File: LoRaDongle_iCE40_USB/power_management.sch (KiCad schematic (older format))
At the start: 17 parts

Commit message: initial changes to iCE40UP5k
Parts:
- removed C? (x2): 1uF, symbol Device:C
- removed U?: AP7331-10WG-7, symbol LoRaDongle:AP7331-10WG-7
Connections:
- net labels removed: 1V
- wire segments 66 -> 53
- no-connect marks 1 -> 0
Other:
- moved on the sheet: C?, D?, L?, R?, U?

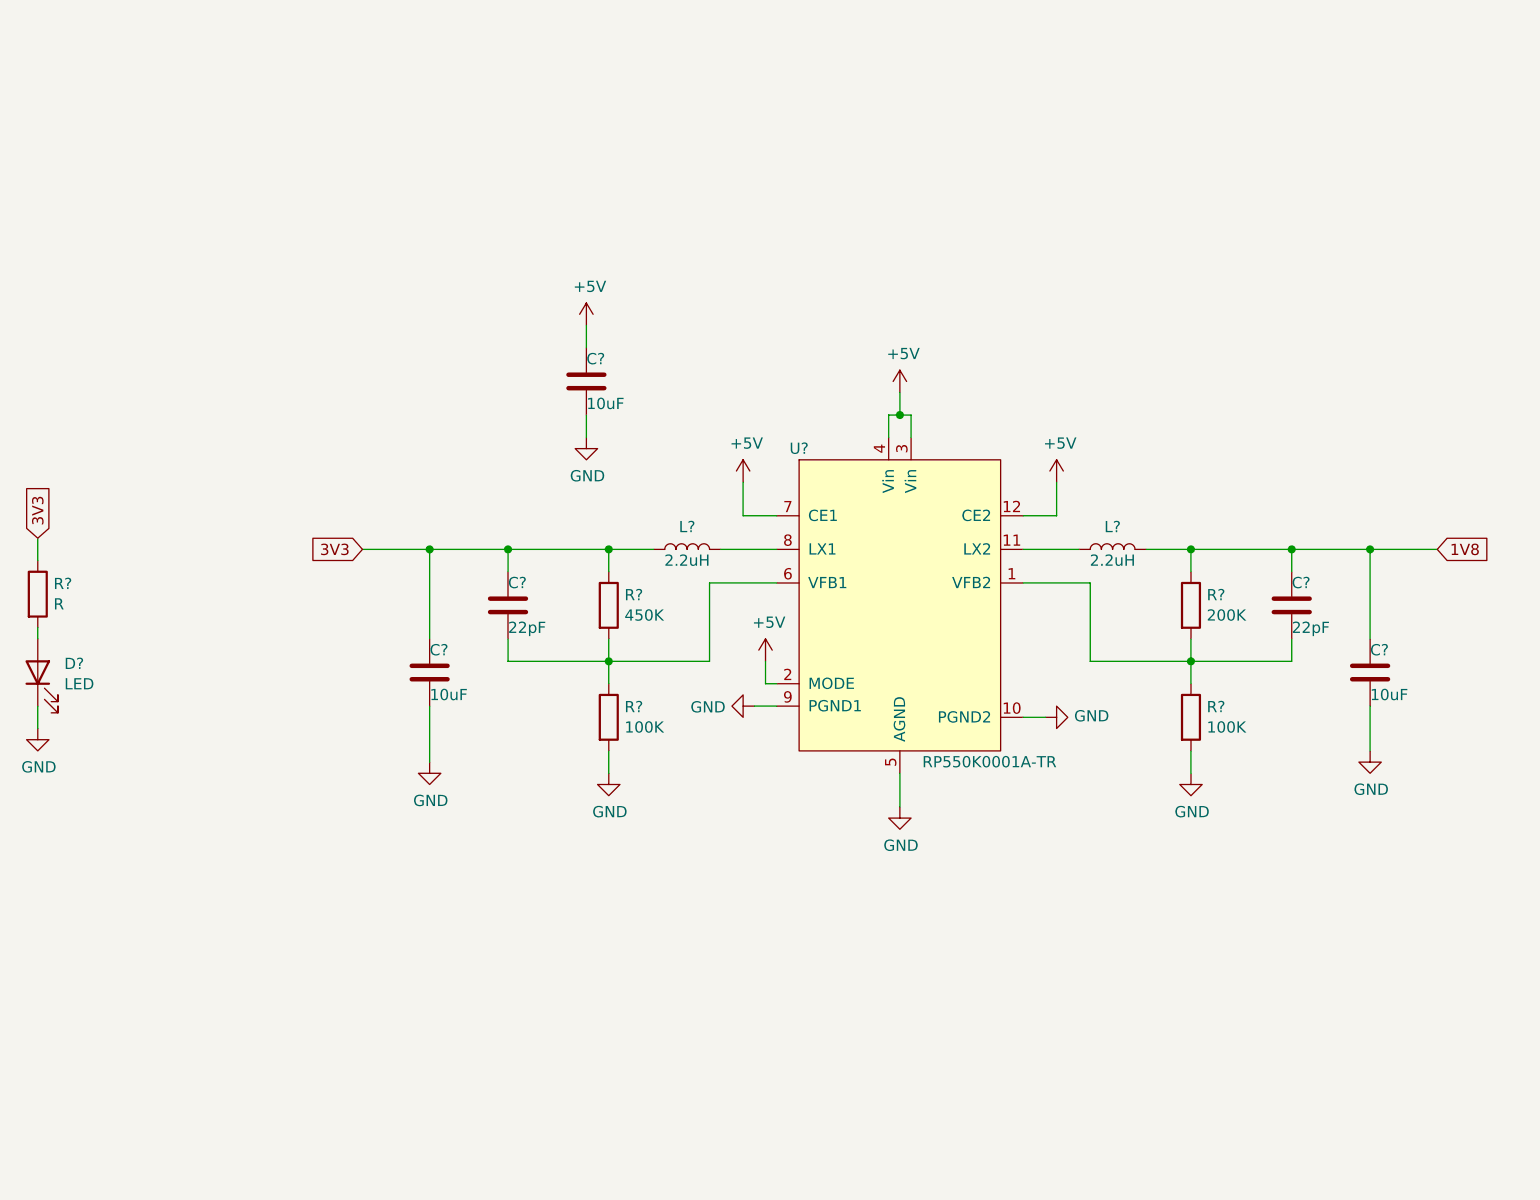
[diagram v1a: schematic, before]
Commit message: changed to sx1261
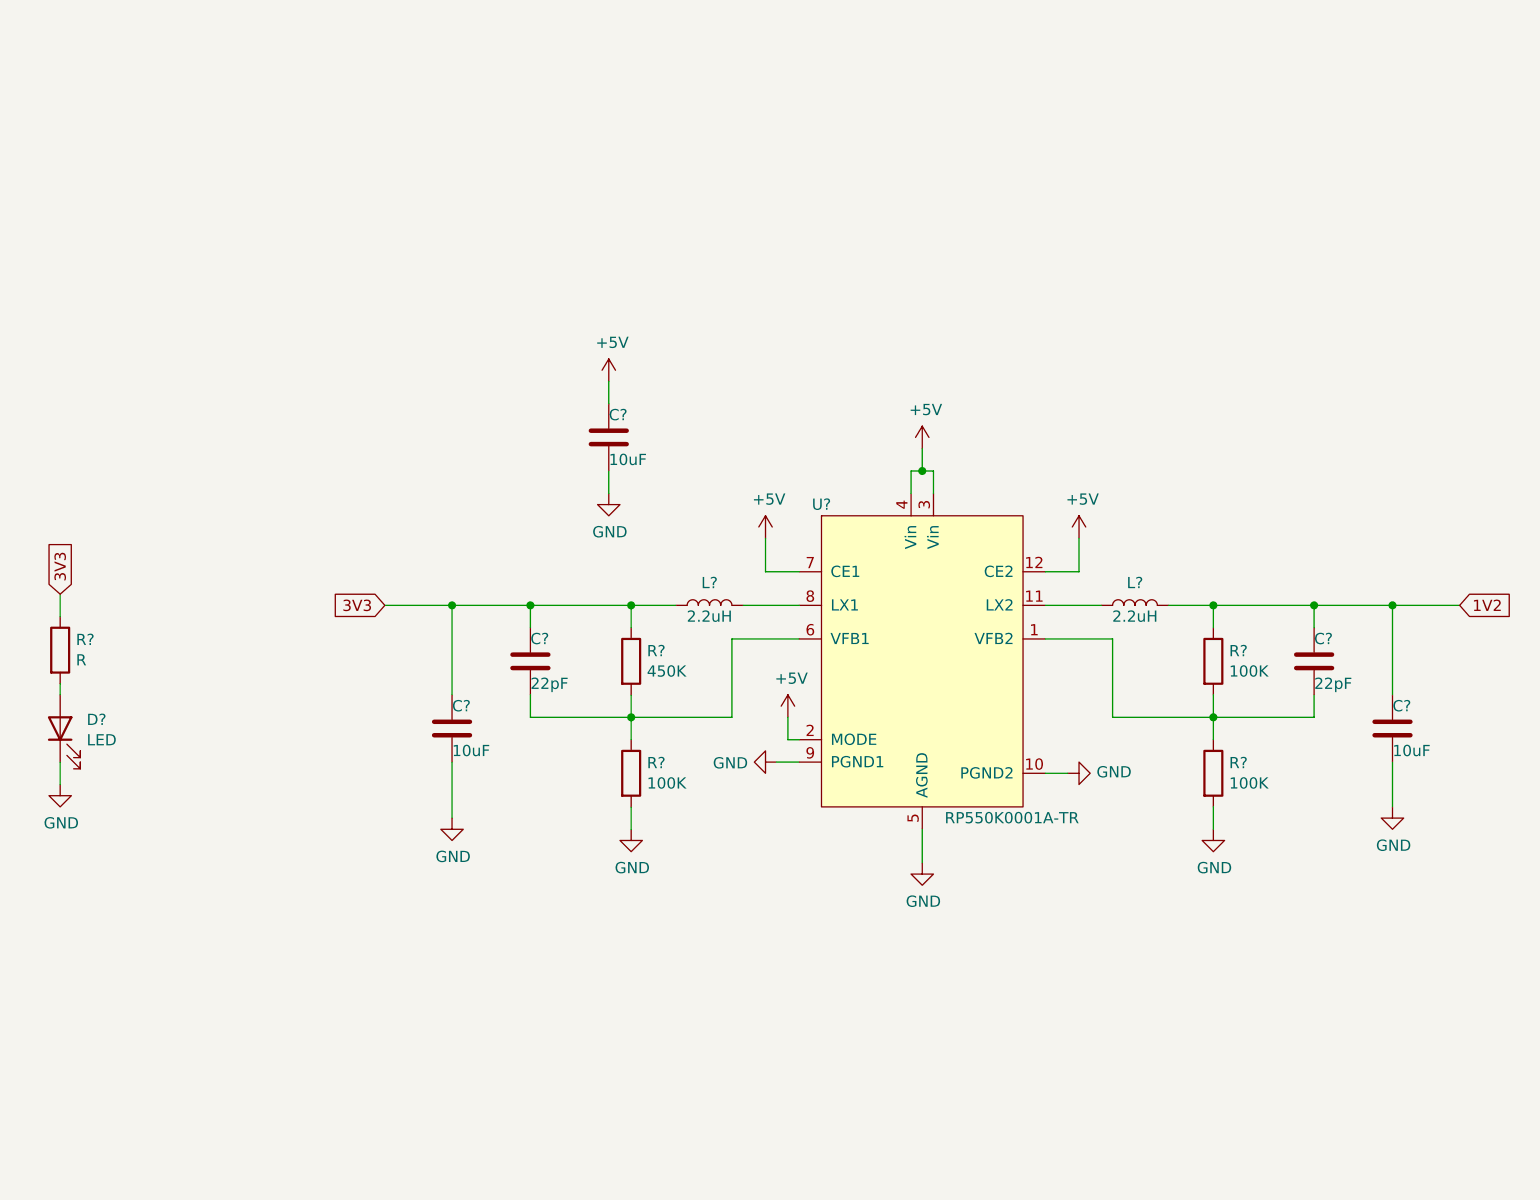
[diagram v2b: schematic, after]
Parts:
- R?: value 200K -> 100K
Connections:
- net 1V8 renamed 1V2
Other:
- moved on the sheet: C?, D?, L?, R?, U?

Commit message: added footprints
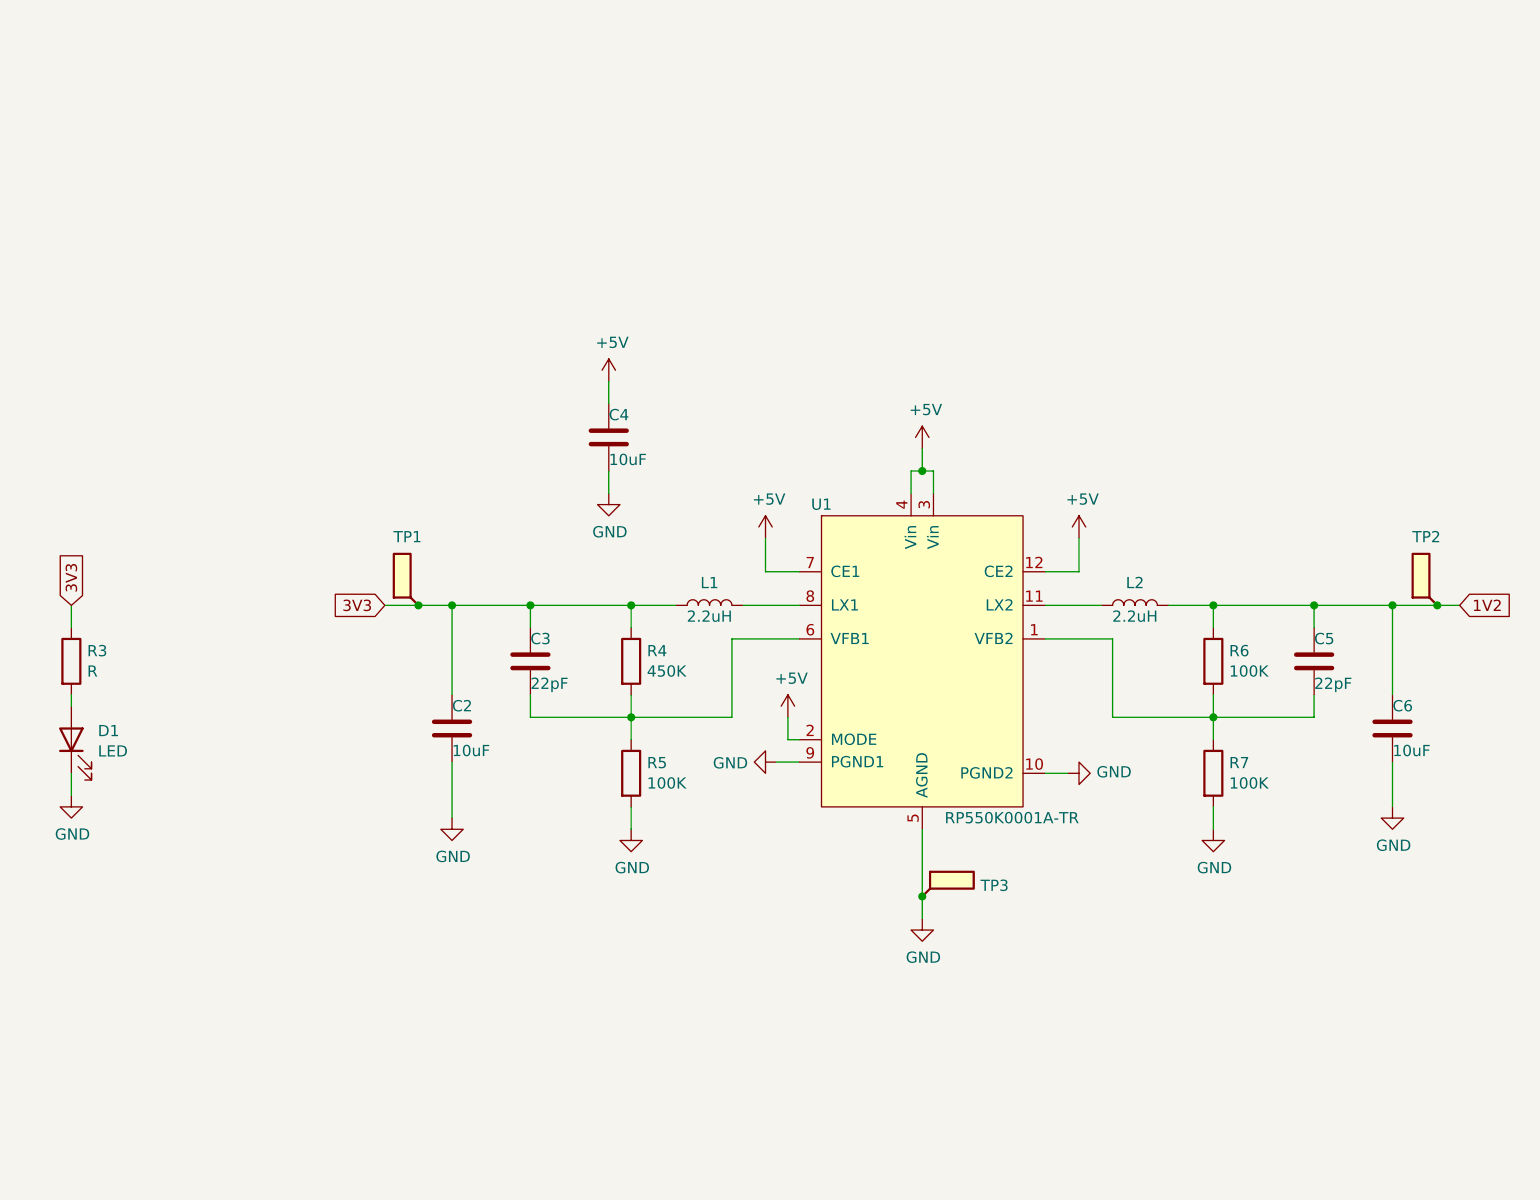
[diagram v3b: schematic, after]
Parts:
- removed C?: 22pF, symbol Device:C
- removed C? (x2): 10uF, Capacitor_SMD:C_0603_1608Metric, symbol Device:C
- removed L? (x2): 2.2uH, symbol Device:L
- added C4, C6: 10uF, Capacitor_SMD:C_0603_1608Metric, symbol Device:C
- added C5: 22pF, Capacitor_SMD:C_01005_0402Metric, symbol Device:C
- added L1, L2: 2.2uH, Inductor_SMD:L_0603_1608Metric, symbol Device:L
- added TP1: 3.3V, TestPoint:TestPoint_Pad_D2.5mm, symbol Connector:TestPoint_Flag
- added TP2: 1.2V, TestPoint:TestPoint_Pad_D2.5mm, symbol Connector:TestPoint_Flag
- added TP3: GND, TestPoint:TestPoint_Pad_D2.5mm, symbol Connector:TestPoint_Flag
- C2: renamed from C?; Part Number C1608JB1A106M080AC -> GRM188R61E106KA73J
- C3: renamed from C?; footprint (none) -> Capacitor_SMD:C_01005_0402Metric; Part Number (none) -> GRM1555C1H220FA01D
- D1: renamed from D?; footprint (none) -> LED_SMD:LED_0603_1608Metric
- R3, R4, R5, R6, R7: renamed from R?; footprint (none) -> Resistor_SMD:R_0402_1005Metric
- U1: renamed from U?; footprint (none) -> RP550K001A-TR_KiCad:SON50P270X300X60-13N
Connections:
- net +5V: now also C4.2
- net 1V2: now also C5.2, C6.2, L2.2, TP2.1
- net 3V3: now also L1.1, TP1.1
- net GND: now also C4.1, C6.1, TP3.1
- net at U1.8 (LX1): now also L1.2
- net at R6.2, R7.1, U1.1 (VFB2): now also C5.1
- net at U1.11 (LX2): now also L2.1
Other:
- moved on the sheet: D1, R3

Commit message: PCB Layout V01
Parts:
- 1V2: renamed from TP2; footprint TestPoint:TestPoint_Pad_D2.5mm -> TestPoint:TestPoint_Pad_D1.0mm
- 3V3: renamed from TP1; footprint TestPoint:TestPoint_Pad_D2.5mm -> TestPoint:TestPoint_Pad_D1.0mm
- C2, C4, C6: footprint Capacitor_SMD:C_0603_1608Metric -> Capacitor_SMD:C_0603_1608Metric_Pad1.08x0.95mm_HandSolder
- C3, C5: footprint Capacitor_SMD:C_01005_0402Metric -> Capacitor_SMD:C_0402_1005Metric_Pad0.74x0.62mm_HandSolder
- D1: footprint LED_SMD:LED_0603_1608Metric -> LED_SMD:LED_0603_1608Metric_Pad1.05x0.95mm_HandSolder
- GND2: renamed from TP3; footprint TestPoint:TestPoint_Pad_D2.5mm -> TestPoint:TestPoint_Pad_D1.0mm
- L1, L2: footprint Inductor_SMD:L_0603_1608Metric -> Inductor_SMD:L_0603_1608Metric_Pad1.05x0.95mm_HandSolder
- R3, R4, R5, R6, R7: footprint Resistor_SMD:R_0402_1005Metric -> Resistor_SMD:R_0402_1005Metric_Pad0.72x0.64mm_HandSolder
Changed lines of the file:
@@
 F 0 "R6" H 7320 3796 50  0000 L CNN
 F 1 "100K" H 7320 3705 50  0000 L CNN
-F 2 "Resistor_SMD:R_0402_1005Metric" V 7180 3750 50  0001 C CNN
+F 2 "Resistor_SMD:R_0402_1005Metric_Pad0.72x0.64mm_HandSolder" V 7180 3750 50  0001 C CNN
 F 3 "~" H 7250 3750 50  0001 C CNN
 	1    7250 3750
@@
 F 0 "R7" H 7320 4296 50  0000 L CNN
 F 1 "100K" H 7320 4205 50  0000 L CNN
-F 2 "Resistor_SMD:R_0402_1005Metric" V 7180 4250 50  0001 C CNN
+F 2 "Resistor_SMD:R_0402_1005Metric_Pad0.72x0.64mm_HandSolder" V 7180 4250 50  0001 C CNN
 F 3 "~" H 7250 4250 50  0001 C CNN
 	1    7250 4250
@@
 F 0 "R4" H 4720 3796 50  0000 L CNN
 F 1 "450K" H 4720 3705 50  0000 L CNN
-F 2 "Resistor_SMD:R_0402_1005Metric" V 4580 3750 50  0001 C CNN
+F 2 "Resistor_SMD:R_0402_1005Metric_Pad0.72x0.64mm_HandSolder" V 4580 3750 50  0001 C CNN
 F 3 "~" H 4650 3750 50  0001 C CNN
 	1    4650 3750
@@
 F 0 "R5" H 4720 4296 50  0000 L CNN
 F 1 "100K" H 4720 4205 50  0000 L CNN
-F 2 "Resistor_SMD:R_0402_1005Metric" V 4580 4250 50  0001 C CNN
+F 2 "Resistor_SMD:R_0402_1005Metric_Pad0.72x0.64mm_HandSolder" V 4580 4250 50  0001 C CNN
 F 3 "~" H 4650 4250 50  0001 C CNN
 	1    4650 4250
@@
 F 0 "C3" H 4200 3650 50  0000 R CNN
 F 1 "22pF" H 4200 3850 50  0000 R CNN
-F 2 "Capacitor_SMD:C_01005_0402Metric" H 4238 3600 50  0001 C CNN
+F 2 "Capacitor_SMD:C_0402_1005Metric_Pad0.74x0.62mm_HandSolder" H 4238 3600 50  0001 C CNN
 F 3 "~" H 4200 3750 50  0001 C CNN
 F 4 "GRM1555C1H220FA01D" H 4200 3750 50  0001 C CNN "Part Number"
@@
 F 0 "C2" H 3850 3950 50  0000 R CNN
 F 1 "10uF" H 3850 4150 50  0000 R CNN
-F 2 "Capacitor_SMD:C_0603_1608Metric" H 3888 3900 50  0001 C CNN
+F 2 "Capacitor_SMD:C_0603_1608Metric_Pad1.08x0.95mm_HandSolder" H 3888 3900 50  0001 C CNN
 F 3 "~" H 3850 4050 50  0001 C CNN
 F 4 "GRM188R61E106KA73J" H 3850 4050 50  0001 C CNN "Part Number"
@@
 F 0 "D1" V 2189 3982 50  0000 R CNN
 F 1 "LED" V 2098 3982 50  0000 R CNN
-F 2 "LED_SMD:LED_0603_1608Metric" H 2150 4100 50  0001 C CNN
+F 2 "LED_SMD:LED_0603_1608Metric_Pad1.05x0.95mm_HandSolder" H 2150 4100 50  0001 C CNN
 F 3 "~" H 2150 4100 50  0001 C CNN
 	1    2150 4100
@@
 F 0 "R3" H 2220 3796 50  0000 L CNN
 F 1 "R" H 2220 3705 50  0000 L CNN
-F 2 "Resistor_SMD:R_0402_1005Metric" V 2080 3750 50  0001 C CNN
+F 2 "Resistor_SMD:R_0402_1005Metric_Pad0.72x0.64mm_HandSolder" V 2080 3750 50  0001 C CNN
 F 3 "~" H 2150 3750 50  0001 C CNN
 	1    2150 3750
@@
 	3550 3500 3700 3500
 $Comp
-L Connector:TestPoint_Flag TP1
+L Connector:TestPoint_Flag 3V3
 U 1 1 61B8BC4D
 P 3700 3500
-F 0 "TP1" V 4005 3548 50  0000 C CNN
+F 0 "3V3" V 4005 3548 50  0000 C CNN
 F 1 "3.3V" V 4006 3548 50  0001 C CNN
-F 2 "TestPoint:TestPoint_Pad_D2.5mm" H 3900 3500 50  0001 C CNN
+F 2 "TestPoint:TestPoint_Pad_D1.0mm" H 3900 3500 50  0001 C CNN
 F 3 "~" H 3900 3500 50  0001 C CNN
 	1    3700 3500
@@
 	3700 3500 3850 3500
 $Comp
-L Connector:TestPoint_Flag TP2
+L Connector:TestPoint_Flag 1V2
 U 1 1 61C195B0
 P 8250 3500
-F 0 "TP2" V 8555 3548 50  0000 C CNN
+F 0 "1V2" V 8555 3548 50  0000 C CNN
 F 1 "1.2V" V 8556 3548 50  0001 C CNN
-F 2 "TestPoint:TestPoint_Pad_D2.5mm" H 8450 3500 50  0001 C CNN
+F 2 "TestPoint:TestPoint_Pad_D1.0mm" H 8450 3500 50  0001 C CNN
 F 3 "~" H 8450 3500 50  0001 C CNN
 	1    8250 3500
@@
 	5950 4500 5950 4800
 $Comp
-L Connector:TestPoint_Flag TP3
+L Connector:TestPoint_Flag GND2
 U 1 1 61C1D032
 P 5950 4800
-F 0 "TP3" H 6210 4848 50  0000 L CNN
+F 0 "GND2" H 6210 4848 50  0000 L CNN
 F 1 "GND" V 6256 4848 50  0001 C CNN
-F 2 "TestPoint:TestPoint_Pad_D2.5mm" H 6150 4800 50  0001 C CNN
+F 2 "TestPoint:TestPoint_Pad_D1.0mm" H 6150 4800 50  0001 C CNN
 F 3 "~" H 6150 4800 50  0001 C CNN
 	1    5950 4800
@@
 F 0 "C6" H 8050 3950 50  0000 R CNN
 F 1 "10uF" H 8050 4150 50  0000 R CNN
-F 2 "Capacitor_SMD:C_0603_1608Metric" H 8088 3900 50  0001 C CNN
+F 2 "Capacitor_SMD:C_0603_1608Metric_Pad1.08x0.95mm_HandSolder" H 8088 3900 50  0001 C CNN
 F 3 "~" H 8050 4050 50  0001 C CNN
 F 4 "GRM188R61E106KA73J" H 8050 4050 50  0001 C CNN "Part Number"
@@
 F 0 "C5" H 7700 3650 50  0000 R CNN
 F 1 "22pF" H 7700 3850 50  0000 R CNN
-F 2 "Capacitor_SMD:C_01005_0402Metric" H 7738 3600 50  0001 C CNN
+F 2 "Capacitor_SMD:C_0402_1005Metric_Pad0.74x0.62mm_HandSolder" H 7738 3600 50  0001 C CNN
 F 3 "~" H 7700 3750 50  0001 C CNN
 F 4 "GRM1555C1H220FA01D" H 7700 3750 50  0001 C CNN "Part Number"
@@
 F 0 "C4" H 4550 2650 50  0000 R CNN
 F 1 "10uF" H 4550 2850 50  0000 R CNN
-F 2 "Capacitor_SMD:C_0603_1608Metric" H 4588 2600 50  0001 C CNN
+F 2 "Capacitor_SMD:C_0603_1608Metric_Pad1.08x0.95mm_HandSolder" H 4588 2600 50  0001 C CNN
 F 3 "~" H 4550 2750 50  0001 C CNN
 F 4 "GRM188R61E106KA73J" H 4550 2750 50  0001 C CNN "Part Number"
@@
 F 0 "L2" V 7000 3500 50  0000 C CNN
 F 1 "2.2uH" V 6850 3500 50  0000 C CNN
-F 2 "Inductor_SMD:L_0603_1608Metric" H 6900 3500 50  0001 C CNN
+F 2 "Inductor_SMD:L_0603_1608Metric_Pad1.05x0.95mm_HandSolder" H 6900 3500 50  0001 C CNN
 F 3 "~" H 6900 3500 50  0001 C CNN
 F 4 "MCHK1608T2R2MKN" V 6900 3500 50  0001 C CNN "Part Number"
@@
 F 0 "L1" V 5100 3500 50  0000 C CNN
 F 1 "2.2uH" V 4950 3500 50  0000 C CNN
-F 2 "Inductor_SMD:L_0603_1608Metric" H 5000 3500 50  0001 C CNN
+F 2 "Inductor_SMD:L_0603_1608Metric_Pad1.05x0.95mm_HandSolder" H 5000 3500 50  0001 C CNN
 F 3 "~" H 5000 3500 50  0001 C CNN
 F 4 "MCHK1608T2R2MKN" V 5000 3500 50  0001 C CNN "Part Number"
